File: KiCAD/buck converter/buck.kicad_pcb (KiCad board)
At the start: 2 copper layers, 44.5 x 27.3 mm, 17 parts, among them P1 VIN, P2 VOUT, Q1 Q_PMOS_DGS, U1 LTC1771

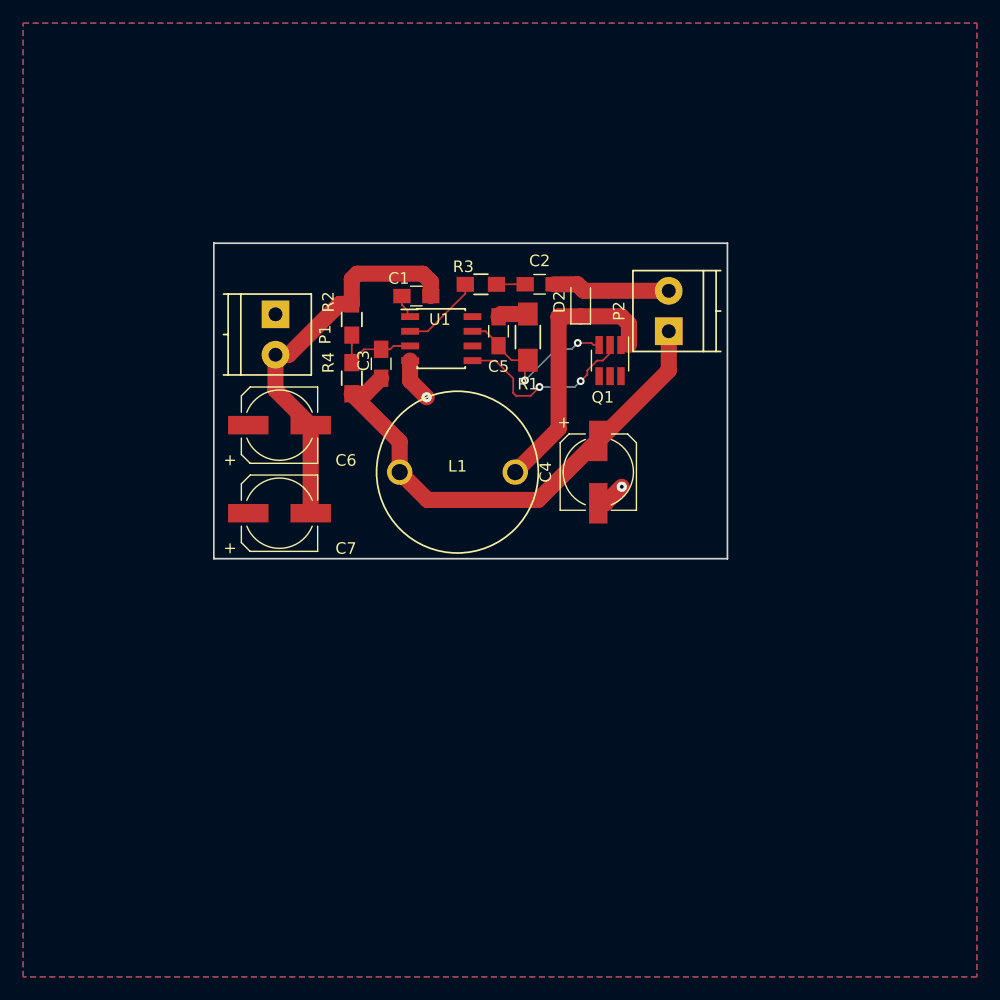
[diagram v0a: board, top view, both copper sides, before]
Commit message: Improved the buck converter board layout
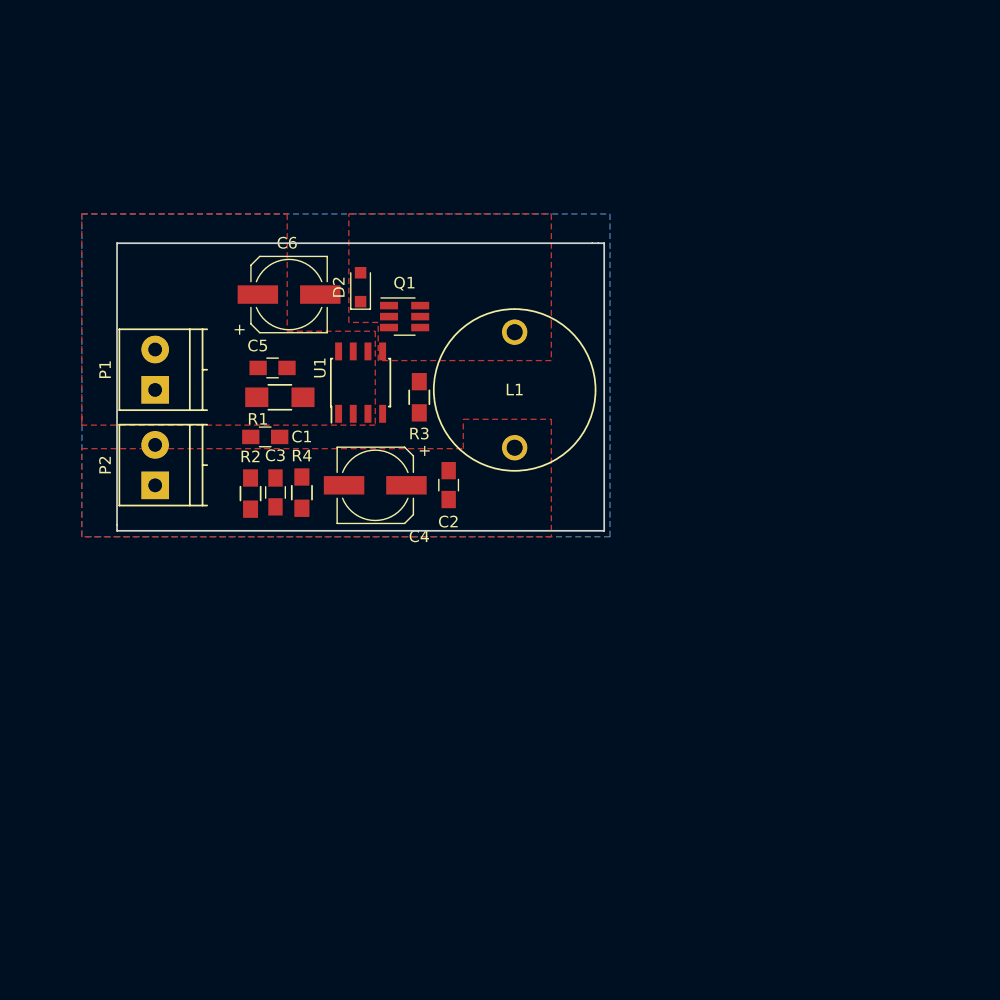
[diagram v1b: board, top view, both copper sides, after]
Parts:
- removed C7: 22uF, Capacitors_SMD:CP_Elec_6.3x5.3
- moved P2 46.4 mm to (113.0, 109.9)
- moved R1 22.1 mm to (123.8, 102.2), turned to 0 degrees
- moved C5 19.8 mm to (123.2, 99.7), turned to 180 degrees
- moved C4 19.3 mm to (132.1, 109.9), turned to 180 degrees
- moved D2 19.1 mm to (130.8, 92.7)
- moved C2 19.1 mm to (138.4, 109.8), turned to 270 degrees
- moved Q1 18.2 mm to (134.6, 95.2), turned to 0 degrees
- moved C1 17.9 mm to (122.6, 105.7), turned to 180 degrees
- moved R2 17.4 mm to (121.3, 110.6), turned to 270 degrees
- moved C3 14.4 mm to (123.4, 110.5)
- moved P1 12.3 mm to (113.0, 101.6), turned to 90 degrees
- moved C6 11.3 mm to (124.6, 93.3)
- moved R3 11.1 mm to (135.9, 102.2), turned to 270 degrees
- moved R4 10.8 mm to (125.7, 110.5)
- moved L1 8.67 mm to (144.1, 101.6), turned to 270 degrees
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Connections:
- net Net-(C1-Pad1) renamed /RUN/SS
- net Net-(C5-Pad1) renamed /SENSE
- net Net-(Q1-Pad2) renamed /GATE
- net Net-(R3-Pad1) renamed /Ith
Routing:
- net GND: track 50.7 -> 0.00 mm, vias 2 -> 0
- net +5V: track 43.9 -> 0.00 mm
- net /Vsw: track 23.2 -> 0.00 mm
- net /GATE: track 16.3 -> 0.00 mm, vias 2 -> 0
- net /SENSE: track 15.7 -> 0.00 mm, vias 2 -> 0
- net Vfb: track 8.08 -> 0.00 mm
- net /Ith: track 6.93 -> 0.00 mm
- net +BATT: track 2.64 -> 0.00 mm
- net Net-(C2-Pad1): track 2.48 -> 0.00 mm
- net /RUN/SS: track 2.07 -> 0.00 mm
- added copper zone on F.Cu, net +5V
- added copper zone on F.Cu, net /Vsw
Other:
- board size 44.5 x 27.3 mm -> 42.2 x 24.9 mm
- net class PWR: clearance 0.1524 -> 1.524; via_dia 0.889 -> 0.6858
- rule pad_to_mask_clearance: 0.2 -> 0

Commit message: Improved silk screen
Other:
- board text added: "+"
- board text added: "-"
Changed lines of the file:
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@@
   (general
     (links 29)
-    (no_connects 22)
-    (area 0 0 0 0)
+    (no_connects 18)
+    (area 106.431 82.14614 159.00642 116.814)
     (thickness 1.6)
-    (drawings 9)
+    (drawings 13)
     (tracks 0)
     (zones 0)
@@
   (page A4)
   (layers
-    (0 F.Cu signal)
+    (0 F.Cu signal hide)
     (31 B.Cu signal)
     (32 B.Adhes user)
@@
       (effects (font (size 1 1) (thickness 0.15)))
     )
-    (fp_text value VIN (at 1.75 6 90) (layer F.Fab)
+    (fp_text value VIN (at 1.75 6 90) (layer F.SilkS)
       (effects (font (size 1 1) (thickness 0.15)))
     )
@@
       (effects (font (size 1 1) (thickness 0.15)))
     )
-    (fp_text value VOUT (at 1.75 6 90) (layer F.Fab)
+    (fp_text value VOUT (at 1.75 6 90) (layer F.SilkS)
       (effects (font (size 1 1) (thickness 0.15)))
     )
@@
     )
   )
+  (gr_text - (at 118.364 97.028 90) (layer F.SilkS)
+    (effects (font (size 0.8128 0.8128) (thickness 0.0762)))
+  )
+  (gr_text - (at 118.364 105.156 90) (layer F.SilkS)
+    (effects (font (size 0.8128 0.8128) (thickness 0.0762)))
+  )
+  (gr_text + (at 118.364 111.252) (layer F.SilkS)
+    (effects (font (size 0.8128 0.8128) (thickness 0.0762)))
+  )
+  (gr_text + (at 118.364 102.616) (layer F.SilkS)
+    (effects (font (size 0.8128 0.8128) (thickness 0.0762)))
+  )
   (dimension 24.892 (width 0.0762) (layer Eco1.User)

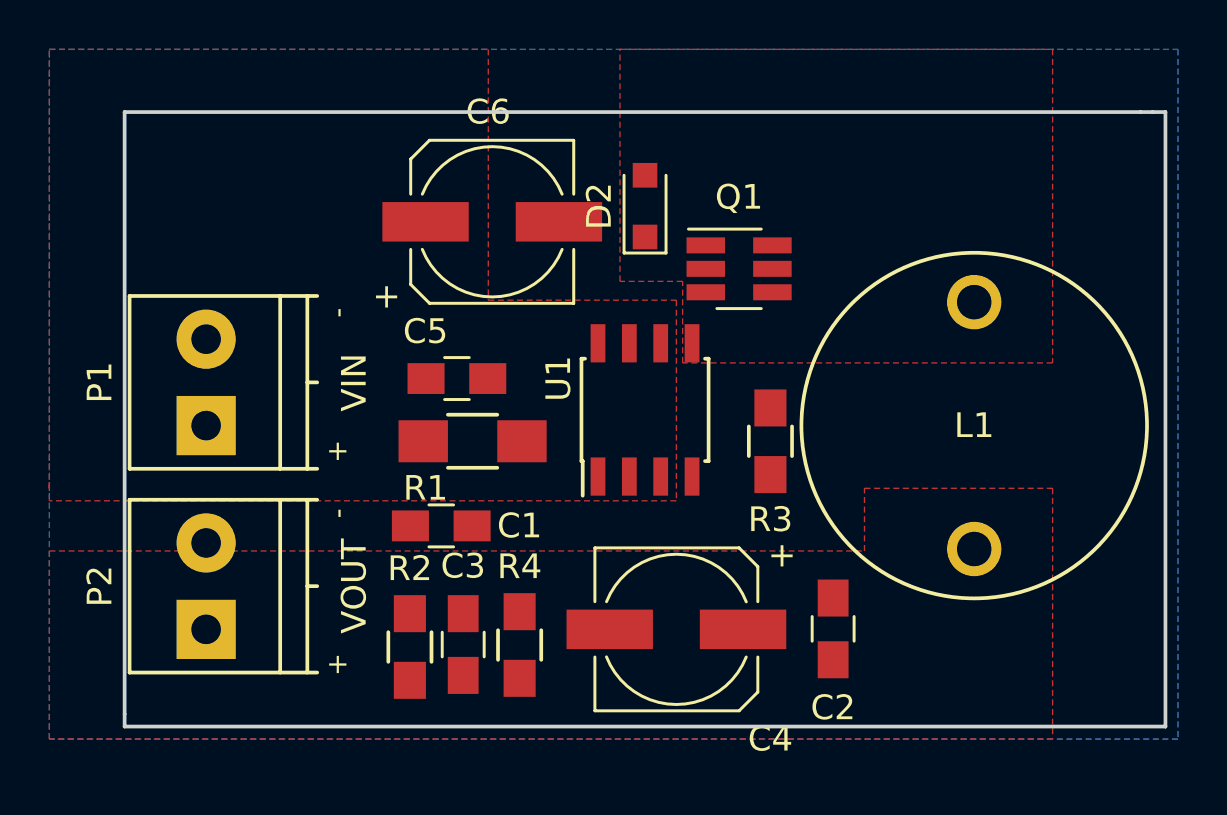
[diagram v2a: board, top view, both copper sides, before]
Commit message: Finished PCB layout for buck converter
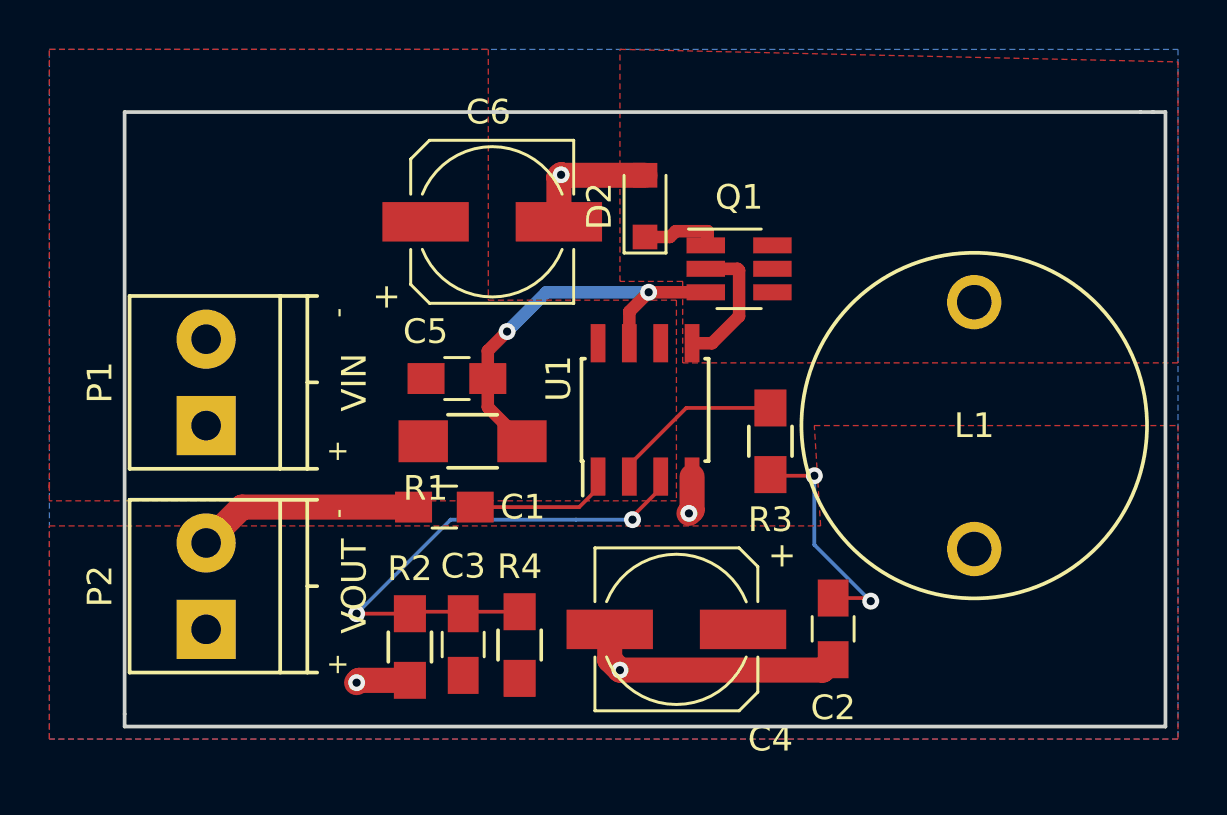
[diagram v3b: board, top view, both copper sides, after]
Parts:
- moved C1 0.77 mm to (122.7, 104.9)
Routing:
- net GND: track 0.00 -> 28.7 mm, vias 0 -> 4
- net Vfb: track 0.00 -> 22.2 mm, vias 0 -> 2
- net /SENSE: track 0.00 -> 16.4 mm, vias 0 -> 2
- net Net-(C2-Pad1): track 0.00 -> 9.40 mm, vias 0 -> 2
- net /Ith: track 0.00 -> 7.14 mm
- net /RUN/SS: track 0.00 -> 5.76 mm
- net /GATE: track 0.00 -> 5.59 mm
- net /Vsw: track 0.00 -> 3.24 mm
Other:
- net class HI_C added: clearance 0.1524, trace_width 0.508, via_dia 0.6858, via_drill 0.3302
- net class PWR: clearance 1.524 -> 0.1524; trace_width 1.397 -> 1.016
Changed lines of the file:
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@@
-(kicad_pcb (version 4) (host pcbnew 4.0.3-stable)
+(kicad_pcb (version 4) (host pcbnew 4.0.5)
   (general
     (links 29)
     (no_connects 18)
-    (area 106.431 82.14614 159.00642 116.814)
+    (area 109.652999 88.824999 151.967001 113.867001)
     (thickness 1.6)
     (drawings 13)
-    (tracks 0)
+    (tracks 65)
     (zones 0)
     (modules 16)
@@
   (page A4)
   (layers
-    (0 F.Cu signal hide)
+    (0 F.Cu signal)
     (31 B.Cu signal)
     (32 B.Adhes user)
@@
     (uvia_dia 0.762)
     (uvia_drill 0.508)
-    (add_net +5V)
-    (add_net +BATT)
-    (add_net /GATE)
     (add_net /Ith)
     (add_net /RUN/SS)
-    (add_net /SENSE)
-    (add_net /Vsw)
-    (add_net GND)
     (add_net "Net-(C2-Pad1)")
     (add_net Vfb)
   )
-  (net_class PWR ""
-    (clearance 1.524)
-    (trace_width 1.397)
+  (net_class HI_C ""
+    (clearance 0.1524)
+    (trace_width 0.508)
     (via_dia 0.6858)
     (via_drill 0.3302)
     (uvia_dia 0.762)
     (uvia_drill 0.508)
+    (add_net /GATE)
+    (add_net /SENSE)
+    (add_net /Vsw)
+  )
+  (net_class PWR ""
+    (clearance 0.1524)
+    (trace_width 1.016)
+    (via_dia 0.6858)
+    (via_drill 0.3302)
+    (uvia_dia 0.762)
+    (uvia_drill 0.508)
+    (add_net +5V)
+    (add_net +BATT)
+    (add_net GND)
   )
   (module Capacitors_SMD:C_0805_HandSoldering (layer F.Cu)
-    (at 122.555 105.664 180)
+    (at 122.682 104.902 180)
     (descr "Capacitor SMD 0805, hand soldering")
     (tags "capacitor 0805")
@@
   (gr_line (start 109.728 88.9) (end 150.876 88.9) (layer Edge.Cuts) (width 0.15))
   (gr_line (start 109.728 113.284) (end 109.728 88.9) (layer Edge.Cuts) (width 0.15))
+  (segment (start 121.285 111.92) (end 119.22 111.92) (width 1.016) (layer F.Cu) (net 1))
+  (segment (start 119.22 111.92) (end 119.126 112.014) (width 1.016) (layer F.Cu) (net 1))
+  (via (at 119.126 112.014) (size 0.6858) (drill 0.3302) (layers F.Cu B.Cu) (net 1))
+  (segment (start 121.432 104.902) (end 114.483 104.902) (width 1.016) (layer F.Cu) (net 1))
+  (segment (start 114.483 104.902) (end 113.03 106.355) (width 1.016) (layer F.Cu) (net 1))
+  (segment (start 138.43 111.085) (end 138.009 111.506) (width 1.016) (layer F.Cu) (net 1))
+  (segment (start 138.009 111.506) (end 129.794 111.506) (width 1.016) (layer F.Cu) (net 1))
+  (segment (start 129.38 109.855) (end 129.38 111.092) (width 1.016) (layer F.Cu) (net 1))
+  (segment (start 129.38 111.092) (end 129.794 111.506) (width 1.016) (layer F.Cu) (net 1))
+  (via (at 129.794 111.506) (size 0.6858) (drill 0.3302) (layers F.Cu B.Cu) (net 1))
+  (segment (start 132.715 103.665) (end 132.715 105.029) (width 1.016) (layer F.Cu) (net 1))
+  (segment (start 132.715 105.029) (end 132.588 105.156) (width 1.016) (layer F.Cu) (net 1))
+  (via (at 132.588 105.156) (size 0.6858) (drill 0.3302) (layers F.Cu B.Cu) (net 1))
+  (via (at 127.409 91.44) (size 0.6858) (drill 0.3302) (layers F.Cu B.Cu) (net 1))
+  (segment (start 130.81 91.46) (end 127.429 91.46) (width 1.016) (layer F.Cu) (net 1))
+  (segment (start 127.429 91.46) (end 127.409 91.44) (width 1.016) (layer F.Cu) (net 1))
+  (segment (start 127.32 93.345) (end 127.32 91.529) (width 1.016) (layer F.Cu) (net 1))
+  (segment (start 127.32 91.529) (end 127.409 91.44) (width 1.016) (layer F.Cu) (net 1))
+  (segment (start 137.668 103.632) (end 135.937 103.632) (width 0.1524) (layer F.Cu) (net 2))
+  (segment (start 135.937 103.632) (end 135.89 103.585) (width 0.1524) (layer F.Cu) (net 2))
+  (segment (start 139.954 108.712) (end 137.668 106.426) (width 0.1524) (layer B.Cu) (net 2))
+  (segment (start 137.668 106.426) (end 137.668 103.632) (width 0.1524) (layer B.Cu) (net 2))
+  (via (at 137.668 103.632) (size 0.6858) (drill 0.3302) (layers F.Cu B.Cu) (net 2))
+  (segment (start 138.43 108.585) (end 139.827 108.585) (width 0.1524) (layer F.Cu) (net 2))
+  (segment (start 139.827 108.585) (end 139.954 108.712) (width 0.1524) (layer F.Cu) (net 2))
+  (via (at 139.954 108.712) (size 0.6858) (drill 0.3302) (layers F.Cu B.Cu) (net 2))
+  (segment (start 119.126 109.22) (end 121.285 109.22) (width 0.1524) (layer F.Cu) (net 4))
+  (segment (start 128.016 105.41) (end 122.936 105.41) (width 0.1524) (layer B.Cu) (net 4))
+  (segment (start 122.936 105.41) (end 119.126 109.22) (width 0.1524) (layer B.Cu) (net 4))
+  (via (at 119.126 109.22) (size 0.6858) (drill 0.3302) (layers F.Cu B.Cu) (net 4))
+  (segment (start 130.302 105.41) (end 128.016 105.41) (width 0.1524) (layer B.Cu) (net 4))
+  (segment (start 131.445 103.665) (end 131.445 104.14) (width 0.1524) (layer F.Cu) (net 4))
+  (segment (start 131.445 104.14) (end 130.302 105.283) (width 0.1524) (layer F.Cu) (net 4))
+  (segment (start 130.302 105.283) (end 130.302 105.41) (width 0.1524) (layer F.Cu) (net 4))
+  (via (at 130.302 105.41) (size 0.6858) (drill 0.3302) (layers F.Cu B.Cu) (net 4))
+  (segment (start 125.73 109.14) (end 121.365 109.14) (width 0.1524) (layer F.Cu) (net 4))
+  (segment (start 121.365 109.14) (end 121.285 109.22) (width 0.1524) (layer F.Cu) (net 4))
+  (segment (start 131.445 104.2274) (end 131.445 103.665) (width 0.1524) (layer F.Cu) (net 4))
+  (segment (start 133.35 93.726) (end 133.35 94.22) (width 0.508) (layer F.Cu) (net 6))
+  (segment (start 133.35 94.22) (end 133.27 94.3) (width 0.508) (layer F.Cu) (net 6))
+  (segment (start 132.052 93.726) (end 133.35 93.726) (width 0.508) (layer F.Cu) (net 6))
+  (segment (start 130.81 93.96) (end 131.818 93.96) (width 0.508) (layer F.Cu) (net 6))
+  (segment (start 131.818 93.96) (end 132.052 93.726) (width 0.508) (layer F.Cu) (net 6))
+  (segment (start 123.932 104.902) (end 128.143 104.902) (width 0.1524) (layer F.Cu) (net 7))
+  (segment (start 128.143 104.902) (end 128.905 104.14) (width 0.1524) (layer F.Cu) (net 7))
+  (segment (start 128.905 104.14) (end 128.905 103.665) (width 0.1524) (layer F.Cu) (net 7))
+  (segment (start 125.222 97.79) (end 126.812 96.2) (width 0.508) (layer B.Cu) (net 8))
+  (segment (start 126.812 96.2) (end 130.957 96.2) (width 0.508) (layer B.Cu) (net 8))
+  (via (at 130.957 96.2) (size 0.6858) (drill 0.3302) (layers F.Cu B.Cu) (net 8))
+  (segment (start 124.44 99.695) (end 124.44 98.572) (width 0.508) (layer F.Cu) (net 8))
+  (segment (start 124.44 98.572) (end 125.222 97.79) (width 0.508) (layer F.Cu) (net 8))
+  (via (at 125.222 97.79) (size 0.6858) (drill 0.3302) (layers F.Cu B.Cu) (net 8))
+  (segment (start 124.44 99.695) (end 124.44 100.85) (width 0.508) (layer F.Cu) (net 8))
+  (segment (start 124.44 100.85) (end 125.825 102.235) (width 0.508) (layer F.Cu) (net 8))
+  (segment (start 133.27 96.2) (end 130.957 96.2) (width 0.508) (layer F.Cu) (net 8))
+  (segment (start 130.957 96.2) (end 130.175 96.982) (width 0.508) (layer F.Cu) (net 8))
+  (segment (start 130.175 96.982) (end 130.175 98.265) (width 0.508) (layer F.Cu) (net 8))
+  (segment (start 134.62 97.168) (end 134.62 95.312) (width 0.508) (layer F.Cu) (net 9))
+  (segment (start 134.62 95.312) (end 134.558 95.25) (width 0.508) (layer F.Cu) (net 9))
+  (segment (start 134.558 95.25) (end 133.27 95.25) (width 0.508) (layer F.Cu) (net 9))
+  (segment (start 132.715 98.265) (end 133.523 98.265) (width 0.508) (layer F.Cu) (net 9))
+  (segment (start 133.523 98.265) (end 134.62 97.168) (width 0.508) (layer F.Cu) (net 9))
+  (segment (start 135.89 100.885) (end 132.48 100.885) (width 0.1524) (layer F.Cu) (net 10))
+  (segment (start 132.48 100.885) (end 130.175 103.19) (width 0.1524) (layer F.Cu) (net 10))
+  (segment (start 130.175 103.19) (end 130.175 103.665) (width 0.1524) (layer F.Cu) (net 10))
   (zone (net 5) (net_name +BATT) (layer F.Cu) (hatch edge 0.508)
     (connect_pads (clearance 0.508))
@@
     (polygon
       (pts
-        (xy 106.68 106.68) (xy 139.7 106.68) (xy 139.7 104.14) (xy 147.32 104.14) (xy 147.32 114.3)
+        (xy 106.68 105.664) (xy 137.922 105.664) (xy 137.668 101.6) (xy 152.4 101.6) (xy 152.4 114.3)
         (xy 106.68 114.3)
       )
@@
     (polygon
       (pts
-        (xy 132.334 99.06) (xy 132.334 95.758) (xy 129.794 95.758) (xy 129.794 86.36) (xy 147.32 86.36)
-        (xy 147.32 95.758) (xy 147.32 99.06)
+        (xy 132.334 99.06) (xy 132.334 95.758) (xy 129.794 95.758) (xy 129.794 86.36) (xy 152.4 86.868)
+        (xy 152.4 96.266) (xy 152.4 99.06)
       )
     )
